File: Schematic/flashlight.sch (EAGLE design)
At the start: 2 parts, among them IC1 AMC7135SOT-89

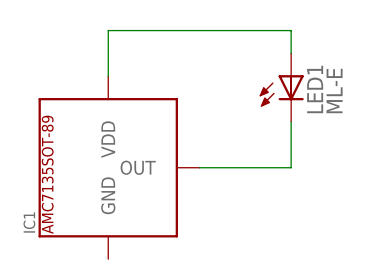
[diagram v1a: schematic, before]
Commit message: Start revision 3.3 by adding a protection diode.
* Add a protection diode for the current regulator.
* Adjust the footprint of the switch to make it slightly easier
  to position and solder.
* Add text for the Diode to the documentation; however it should
  have updated pictures for the board throughout since this is
  more than a cosmetic change.
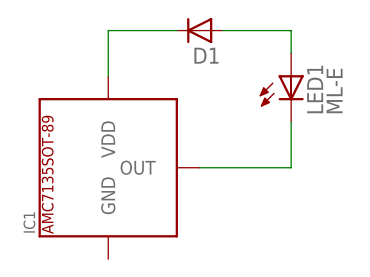
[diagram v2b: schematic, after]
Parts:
- added D1: DIODE-RECTIFIER323, chrisy-components:DIODE-RECTIFIER323
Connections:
- new net N$25: D1.C, IC1.VDD
- net N$28: no longer IC1.VDD
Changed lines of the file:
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@@
 <?xml version="1.0" encoding="utf-8"?>
 <!DOCTYPE eagle SYSTEM "eagle.dtd">
-<eagle version="7.2.0">
+<eagle version="7.3.0">
 <drawing>
 <settings>
@@
 <setting verticaltext="up"/>
 </settings>
-<grid distance="0.1" unitdist="inch" unit="inch" style="lines" multiple="1" display="no" altdistance="0.01" altunitdist="inch" altunit="inch"/>
+<grid distance="0.1" unitdist="inch" unit="inch" style="lines" multiple="1" display="yes" altdistance="0.01" altunitdist="inch" altunit="inch"/>
 <layers>
 <layer number="1" name="Top" color="4" fill="1" visible="no" active="no"/>
@@
 <layer number="48" name="Document" color="7" fill="1" visible="no" active="no"/>
 <layer number="49" name="Reference" color="7" fill="1" visible="no" active="no"/>
+<layer number="50" name="dxf" color="7" fill="1" visible="no" active="no"/>
 <layer number="51" name="tDocu" color="6" fill="9" visible="no" active="no"/>
 <layer number="52" name="bDocu" color="7" fill="1" visible="no" active="no"/>
+<layer number="53" name="tGND_GNDA" color="7" fill="9" visible="no" active="no"/>
+<layer number="54" name="bGND_GNDA" color="1" fill="9" visible="no" active="no"/>
+<layer number="56" name="wert" color="7" fill="1" visible="no" active="no"/>
 <layer number="90" name="Modules" color="5" fill="1" visible="yes" active="yes"/>
 <layer number="91" name="Nets" color="2" fill="1" visible="yes" active="yes"/>
@@
 <layer number="98" name="Guide" color="6" fill="1" visible="yes" active="yes"/>
 <layer number="99" name="SpiceOrder" color="5" fill="1" visible="yes" active="yes"/>
+<layer number="100" name="Muster" color="7" fill="1" visible="no" active="no"/>
+<layer number="101" name="Patch_Top" color="12" fill="4" visible="no" active="yes"/>
+<layer number="102" name="Vscore" color="7" fill="1" visible="no" active="yes"/>
+<layer number="103" name="tMap" color="7" fill="1" visible="no" active="yes"/>
+<layer number="104" name="Name" color="16" fill="1" visible="no" active="yes"/>
+<layer number="105" name="tPlate" color="7" fill="1" visible="no" active="yes"/>
+<layer number="106" name="bPlate" color="7" fill="1" visible="no" active="yes"/>
+<layer number="107" name="Crop" color="7" fill="1" visible="no" active="yes"/>
+<layer number="108" name="tplace-old" color="10" fill="1" visible="yes" active="yes"/>
+<layer number="109" name="ref-old" color="11" fill="1" visible="yes" active="yes"/>
+<layer number="116" name="Patch_BOT" color="9" fill="4" visible="no" active="yes"/>
+<layer number="121" name="_tsilk" color="7" fill="1" visible="no" active="yes"/>
+<layer number="122" name="_bsilk" color="7" fill="1" visible="no" active="yes"/>
+<layer number="125" name="_tNames" color="7" fill="1" visible="no" active="yes"/>
+<layer number="144" name="Drill_legend" color="7" fill="1" visible="no" active="yes"/>
+<layer number="151" name="HeatSink" color="7" fill="1" visible="no" active="yes"/>
+<layer number="199" name="Contour" color="7" fill="1" visible="yes" active="yes"/>
+<layer number="200" name="200bmp" color="1" fill="10" visible="no" active="yes"/>
+<layer number="201" name="201bmp" color="2" fill="10" visible="no" active="yes"/>
+<layer number="202" name="202bmp" color="3" fill="10" visible="no" active="yes"/>
+<layer number="203" name="203bmp" color="4" fill="10" visible="no" active="yes"/>
+<layer number="204" name="204bmp" color="5" fill="10" visible="no" active="yes"/>
+<layer number="205" name="205bmp" color="6" fill="10" visible="no" active="yes"/>
+<layer number="206" name="206bmp" color="7" fill="10" visible="no" active="yes"/>
+<layer number="207" name="207bmp" color="8" fill="10" visible="no" active="yes"/>
+<layer number="208" name="208bmp" color="9" fill="10" visible="no" active="yes"/>
+<layer number="209" name="209bmp" color="7" fill="1" visible="no" active="yes"/>
+<layer number="210" name="210bmp" color="7" fill="1" visible="no" active="yes"/>
+<layer number="211" name="211bmp" color="7" fill="1" visible="no" active="yes"/>
+<layer number="212" name="212bmp" color="7" fill="1" visible="no" active="yes"/>
+<layer number="213" name="213bmp" color="7" fill="1" visible="no" active="yes"/>
+<layer number="214" name="214bmp" color="7" fill="1" visible="no" active="yes"/>
+<layer number="215" name="215bmp" color="7" fill="1" visible="no" active="yes"/>
+<layer number="216" name="216bmp" color="7" fill="1" visible="no" active="yes"/>
+<layer number="217" name="217bmp" color="18" fill="1" visible="no" active="no"/>
+<layer number="218" name="218bmp" color="19" fill="1" visible="no" active="no"/>
+<layer number="219" name="219bmp" color="20" fill="1" visible="no" active="no"/>
+<layer number="220" name="220bmp" color="21" fill="1" visible="no" active="no"/>
+<layer number="221" name="221bmp" color="22" fill="1" visible="no" active="no"/>
+<layer number="222" name="222bmp" color="23" fill="1" visible="no" active="no"/>
+<layer number="223" name="223bmp" color="24" fill="1" visible="no" active="no"/>
+<layer number="224" name="224bmp" color="25" fill="1" visible="no" active="no"/>
+<layer number="250" name="Descript" color="3" fill="1" visible="no" active="no"/>
+<layer number="251" name="SMDround" color="12" fill="11" visible="no" active="no"/>
+<layer number="254" name="cooling" color="7" fill="1" visible="no" active="yes"/>
 </layers>
 <schematic xreflabel="%F%N/%S.%C%R" xrefpart="/%S.%C%R">
@@
 <part name="LED1" library="led" deviceset="ML-E" device=""/>
 <part name="IC1" library="esoteric-regulators" deviceset="AMC7135" device="SOT-89"/>
+<part name="D1" library="chrisy-components" deviceset="DIODE-RECTIFIER" device="323" value=""/>
 </parts>
 <sheets>
@@
 <instance part="LED1" gate="G$1" x="38.1" y="43.18"/>
 <instance part="IC1" gate="G$1" x="10.16" y="27.94"/>
+<instance part="D1" gate="G$1" x="27.94" y="50.8" rot="R180"/>
 </instances>
 <busses>
@@
 <pinref part="LED1" gate="G$1" pin="A@1"/>
 <wire x1="38.1" y1="48.26" x2="38.1" y2="50.8" width="0.1524" layer="91"/>
+<wire x1="38.1" y1="50.8" x2="30.48" y2="50.8" width="0.1524" layer="91"/>
+</segment>
+</net>
+<net name="N$25" class="0">
+<segment>
+<pinref part="D1" gate="G$1" pin="C"/>
 <pinref part="IC1" gate="G$1" pin="VDD"/>
-<wire x1="38.1" y1="50.8" x2="17.78" y2="50.8" width="0.1524" layer="91"/>
+<wire x1="25.4" y1="50.8" x2="17.78" y2="50.8" width="0.1524" layer="91"/>
 <wire x1="17.78" y1="50.8" x2="17.78" y2="45.72" width="0.1524" layer="91"/>
 </segment>
